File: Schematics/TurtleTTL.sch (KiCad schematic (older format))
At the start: 0 parts

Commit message: Review decoupling capacitors again.
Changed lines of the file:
@@
 $EndSheet
 $Sheet
-S 6500 5750 1500 500
+S 4850 5750 1500 500
 U 5D2C13FD
 F0 "Control Word Display" 50
@@
 $EndSheet
 $Sheet
-S 4850 5750 1500 500
+S 3200 5750 1500 500
 U 5D29E36D
 F0 "Register D" 50
@@
 $EndSheet
 $Sheet
-S 3200 5750 1500 500
+S 3200 5050 1500 500
 U 5DD4FB60
 F0 "Serial" 50

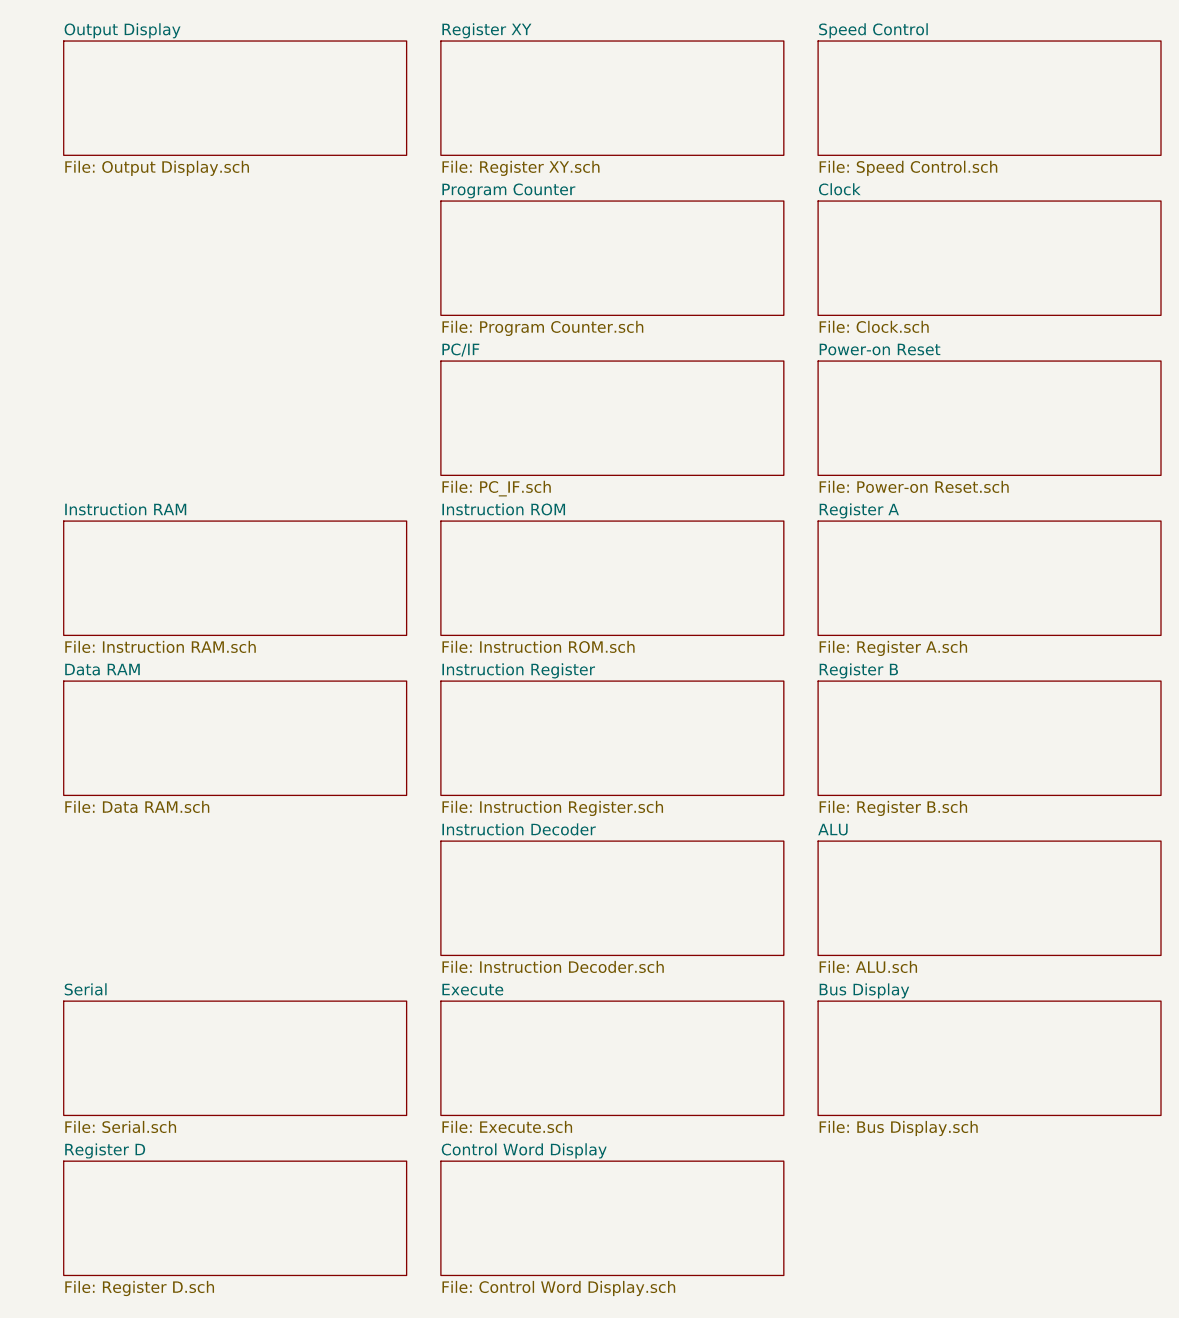
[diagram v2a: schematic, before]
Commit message: Merge the Execute sheet and the Control Word Display sheet.
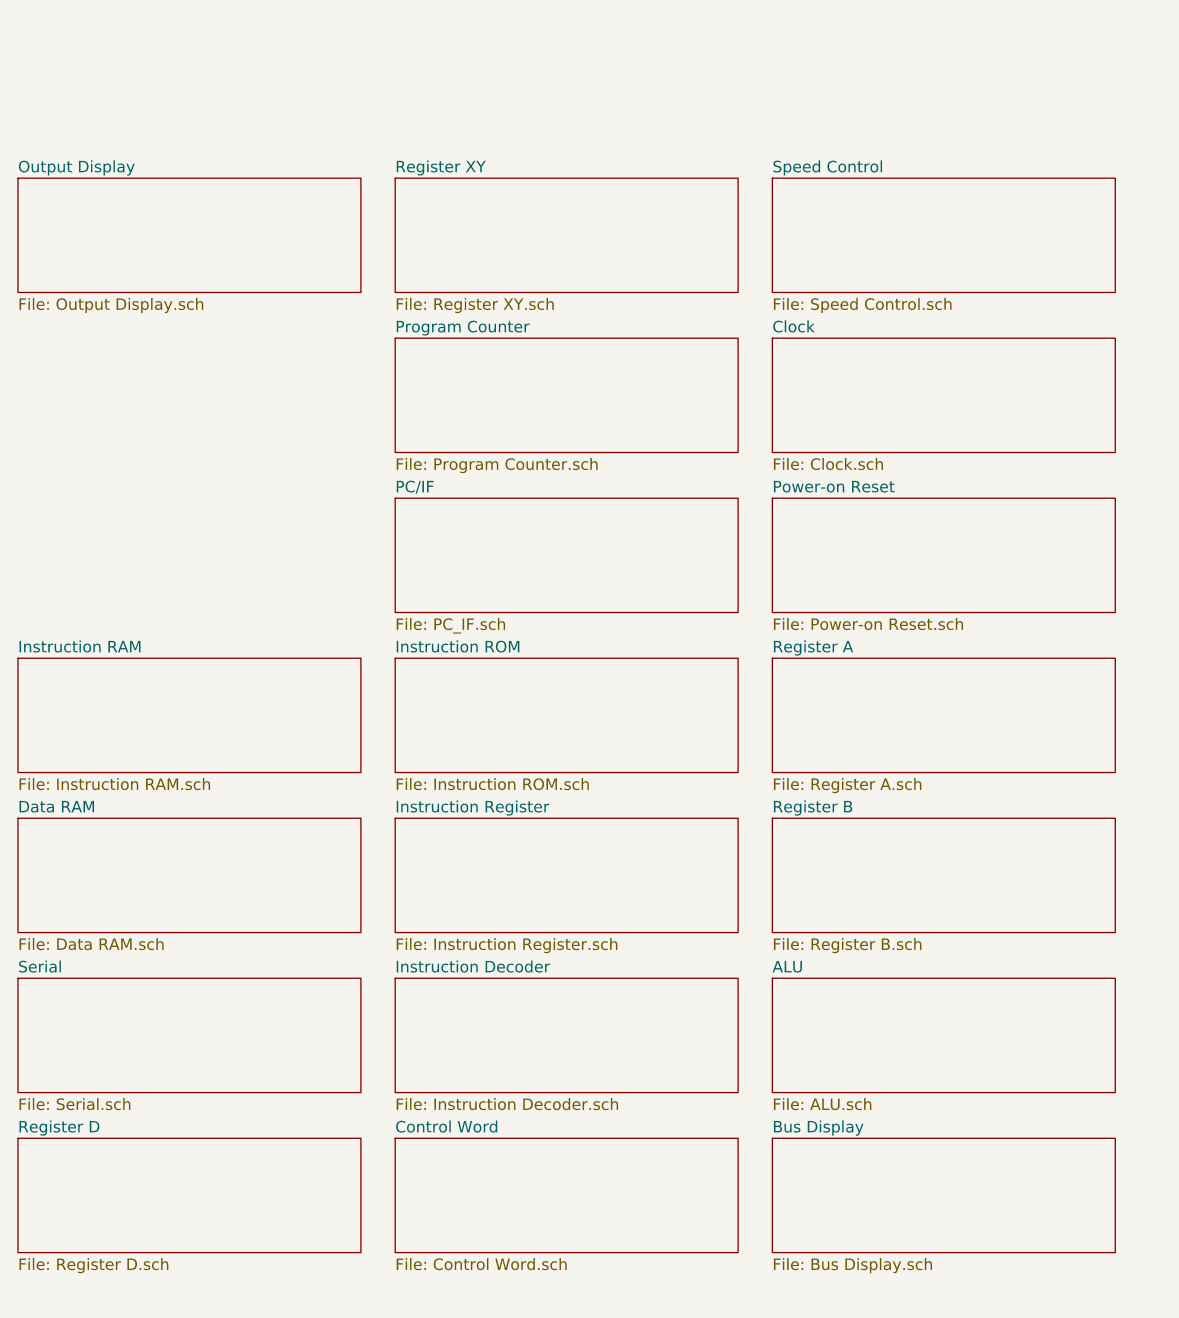
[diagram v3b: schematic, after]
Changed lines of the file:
@@
 $EndDescr
 $Sheet
-S 6500 1550 1500 500
+S 6300 2150 1500 500
 U 5D2C0720
 F0 "Clock" 50
@@
 $EndSheet
 $Sheet
-S 6500 2250 1500 500
+S 6300 2850 1500 500
 U 5D2C0761
 F0 "Power-on Reset" 50
@@
 $EndSheet
 $Sheet
-S 4850 1550 1500 500
+S 4650 2150 1500 500
 U 5D2C07CD
 F0 "Program Counter" 50
@@
 $EndSheet
 $Sheet
-S 4850 2950 1500 500
+S 4650 3550 1500 500
 U 5D2C0AA0
 F0 "Instruction ROM" 50
@@
 $EndSheet
 $Sheet
-S 3200 2950 1500 500
+S 3000 3550 1500 500
 U 5D2C0B01
 F0 "Instruction RAM" 50
@@
 $EndSheet
 $Sheet
-S 4850 4350 1500 500
+S 4650 4950 1500 500
 U 5D2C0B92
 F0 "Instruction Decoder" 50
@@
 $EndSheet
 $Sheet
-S 4850 5050 1500 500
-U 5D2C0BED
-F0 "Execute" 50
-F1 "Execute.sch" 50
-$EndSheet
-$Sheet
-S 3200 850  1500 500
+S 3000 1450 1500 500
 U 5D2C0C74
 F0 "Output Display" 50
@@
 $EndSheet
 $Sheet
-S 6500 2950 1500 500
+S 6300 3550 1500 500
 U 5D2C0CA7
 F0 "Register A" 50
@@
 $EndSheet
 $Sheet
-S 6500 4350 1500 500
+S 6300 4950 1500 500
 U 5D2C0CE4
 F0 "ALU" 50
@@
 $EndSheet
 $Sheet
-S 6500 3650 1500 500
+S 6300 4250 1500 500
 U 5D2C0D13
 F0 "Register B" 50
@@
 $EndSheet
 $Sheet
-S 3200 3650 1500 500
+S 3000 4250 1500 500
 U 5D2C1188
 F0 "Data RAM" 50
@@
 $EndSheet
 $Sheet
-S 6500 5050 1500 500
+S 6300 5650 1500 500
 U 5D2C12A5
 F0 "Bus Display" 50
@@
 $EndSheet
 $Sheet
-S 4850 5750 1500 500
+S 4650 5650 1500 500
 U 5D2C13FD
-F0 "Control Word Display" 50
-F1 "Control Word Display.sch" 50
+F0 "Control Word" 50
+F1 "Control Word.sch" 50
 $EndSheet
 $Sheet
-S 4850 3650 1500 500
+S 4650 4250 1500 500
 U 5D2C14C3
 F0 "Instruction Register" 50
@@
 $EndSheet
 $Sheet
-S 3200 5750 1500 500
+S 3000 5650 1500 500
 U 5D29E36D
 F0 "Register D" 50
@@
 $EndSheet
 $Sheet
-S 6500 850  1500 500
+S 6300 1450 1500 500
 U 5D79C284
 F0 "Speed Control" 50
@@
 $EndSheet
 $Sheet
-S 4850 850  1500 500
+S 4650 1450 1500 500
 U 5D7BD0EA
 F0 "Register XY" 50
@@
 $EndSheet
 $Sheet
-S 4850 2250 1500 500
+S 4650 2850 1500 500
 U 5D7BE200
 F0 "PC/IF" 50
@@
 $EndSheet
 $Sheet
-S 3200 5050 1500 500
+S 3000 4950 1500 500
 U 5DD4FB60
 F0 "Serial" 50

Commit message: Reorganize schematics to show the split between ID and EX more distinctly.
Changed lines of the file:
@@
 S 4650 5650 1500 500
 U 5D2C13FD
-F0 "Control Word" 50
-F1 "Control Word.sch" 50
+F0 "Execute" 50
+F1 "Execute.sch" 50
 $EndSheet
 $Sheet

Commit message: Flesh out Instruction RAM.
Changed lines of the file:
@@
 $Descr A 11000 8500
 encoding utf-8
-Sheet 1 20
+Sheet 1 24
 Title "Turtle TTL"
 Date ""
@@
 $Sheet
 S 4650 3550 1500 500
-U 5D2C0AA0
-F0 "Instruction ROM" 50
-F1 "Instruction ROM.sch" 50
-$EndSheet
-$Sheet
-S 3000 3550 1500 500
-U 5D2C0B01
-F0 "Instruction RAM" 50
-F1 "Instruction RAM.sch" 50
-$EndSheet
-$Sheet
-S 4650 4950 1500 500
 U 5D2C0B92
-F0 "Instruction Decoder" 50
-F1 "Instruction Decoder.sch" 50
+F0 "Instruction Decode" 50
+F1 "Instruction Decode.sch" 50
 $EndSheet
 $Sheet
@@
 $EndSheet
 $Sheet
-S 3000 4250 1500 500
+S 3000 3550 1500 500
 U 5D2C1188
 F0 "Data RAM" 50
@@
 $EndSheet
 $Sheet
-S 6300 5650 1500 500
+S 4650 4950 1500 500
 U 5D2C12A5
 F0 "Bus Display" 50
@@
 $EndSheet
 $Sheet
-S 4650 5650 1500 500
+S 4650 4250 1500 500
 U 5D2C13FD
 F0 "Execute" 50
@@
 $EndSheet
 $Sheet
-S 4650 4250 1500 500
-U 5D2C14C3
-F0 "Instruction Register" 50
-F1 "Instruction Register.sch" 50
-$EndSheet
-$Sheet
-S 3000 5650 1500 500
+S 3000 4950 1500 500
 U 5D29E36D
 F0 "Register D" 50
@@
 $EndSheet
 $Sheet
-S 4650 2850 1500 500
-U 5D7BE200
-F0 "PC/IF" 50
-F1 "PC_IF.sch" 50
-$EndSheet
-$Sheet
-S 3000 4950 1500 500
+S 3000 4250 1500 500
 U 5DD4FB60
 F0 "Serial" 50
 F1 "Serial.sch" 50
 $EndSheet
+$Sheet
+S 4650 2850 1500 500
+U 5D8005AF
+F0 "Instruction Fetch" 50
+F1 "Instruction Fetch.sch" 50
+$EndSheet
 $EndSCHEMATC
